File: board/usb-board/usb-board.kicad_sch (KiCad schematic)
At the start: 16 parts, among them J2 Conn_01x04_Pin, J3 USB_B_Micro, J4 Conn_01x04_Pin, SW1 SW_SPDT, U1 AMS1117-3.3, U2 STM32F103C8T6, Y1 8Mhz

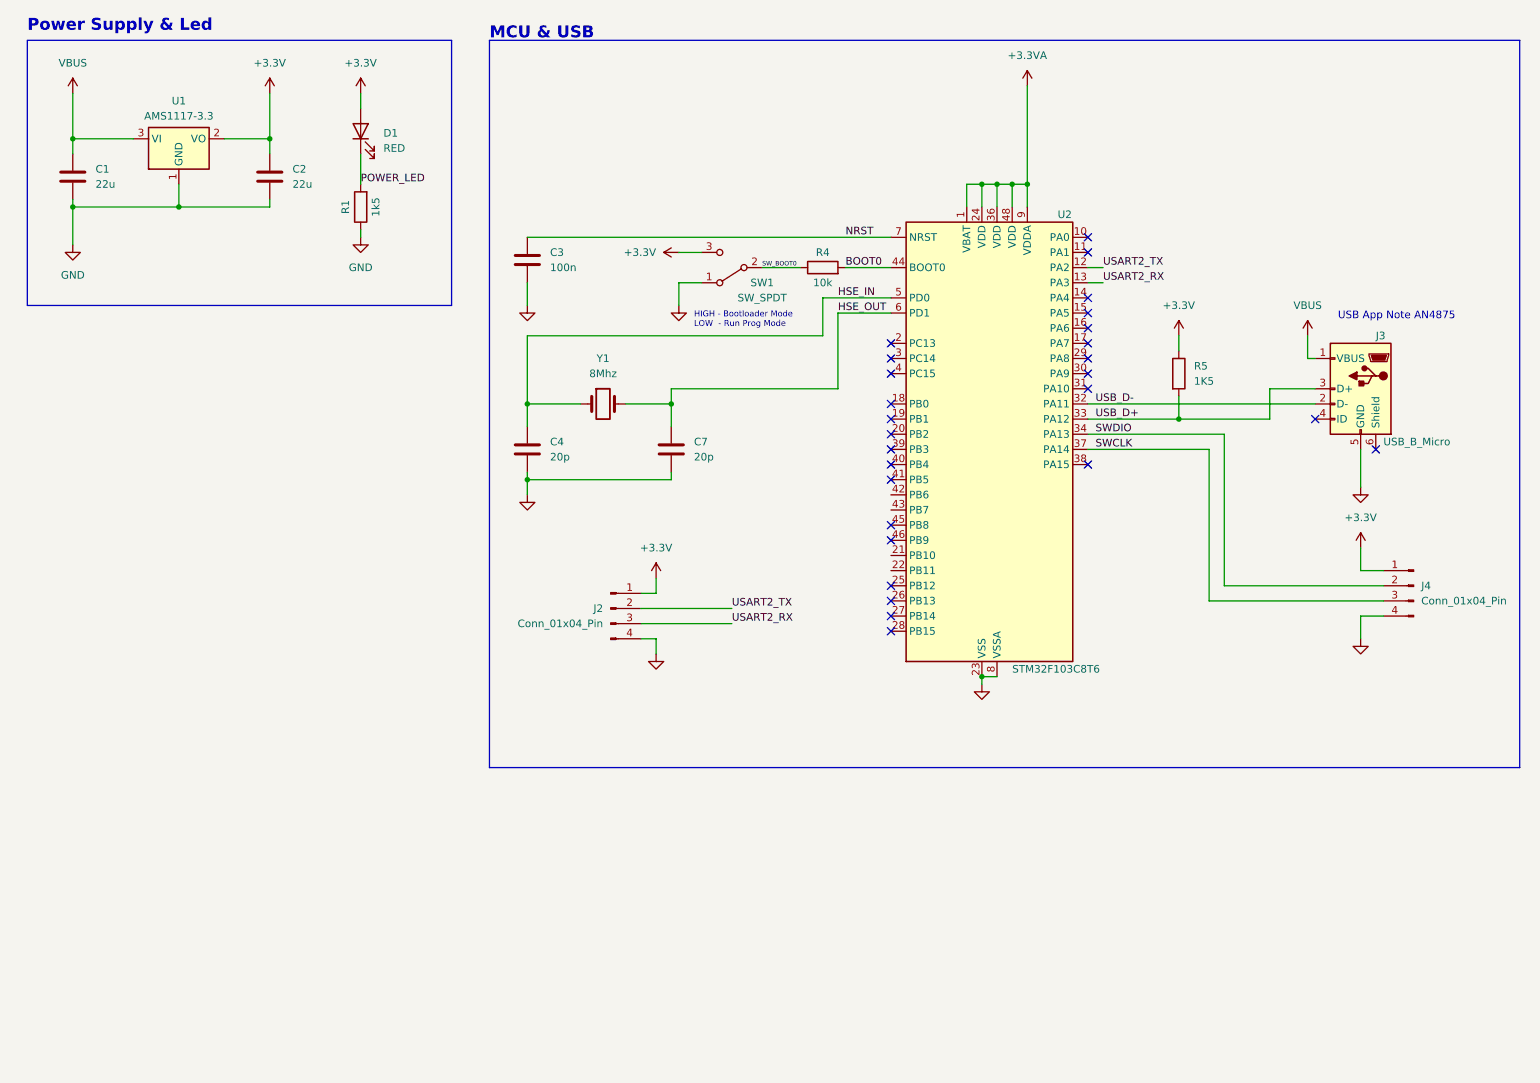
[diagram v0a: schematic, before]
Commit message: [ADD] Add transceiver on scheme for RS-485
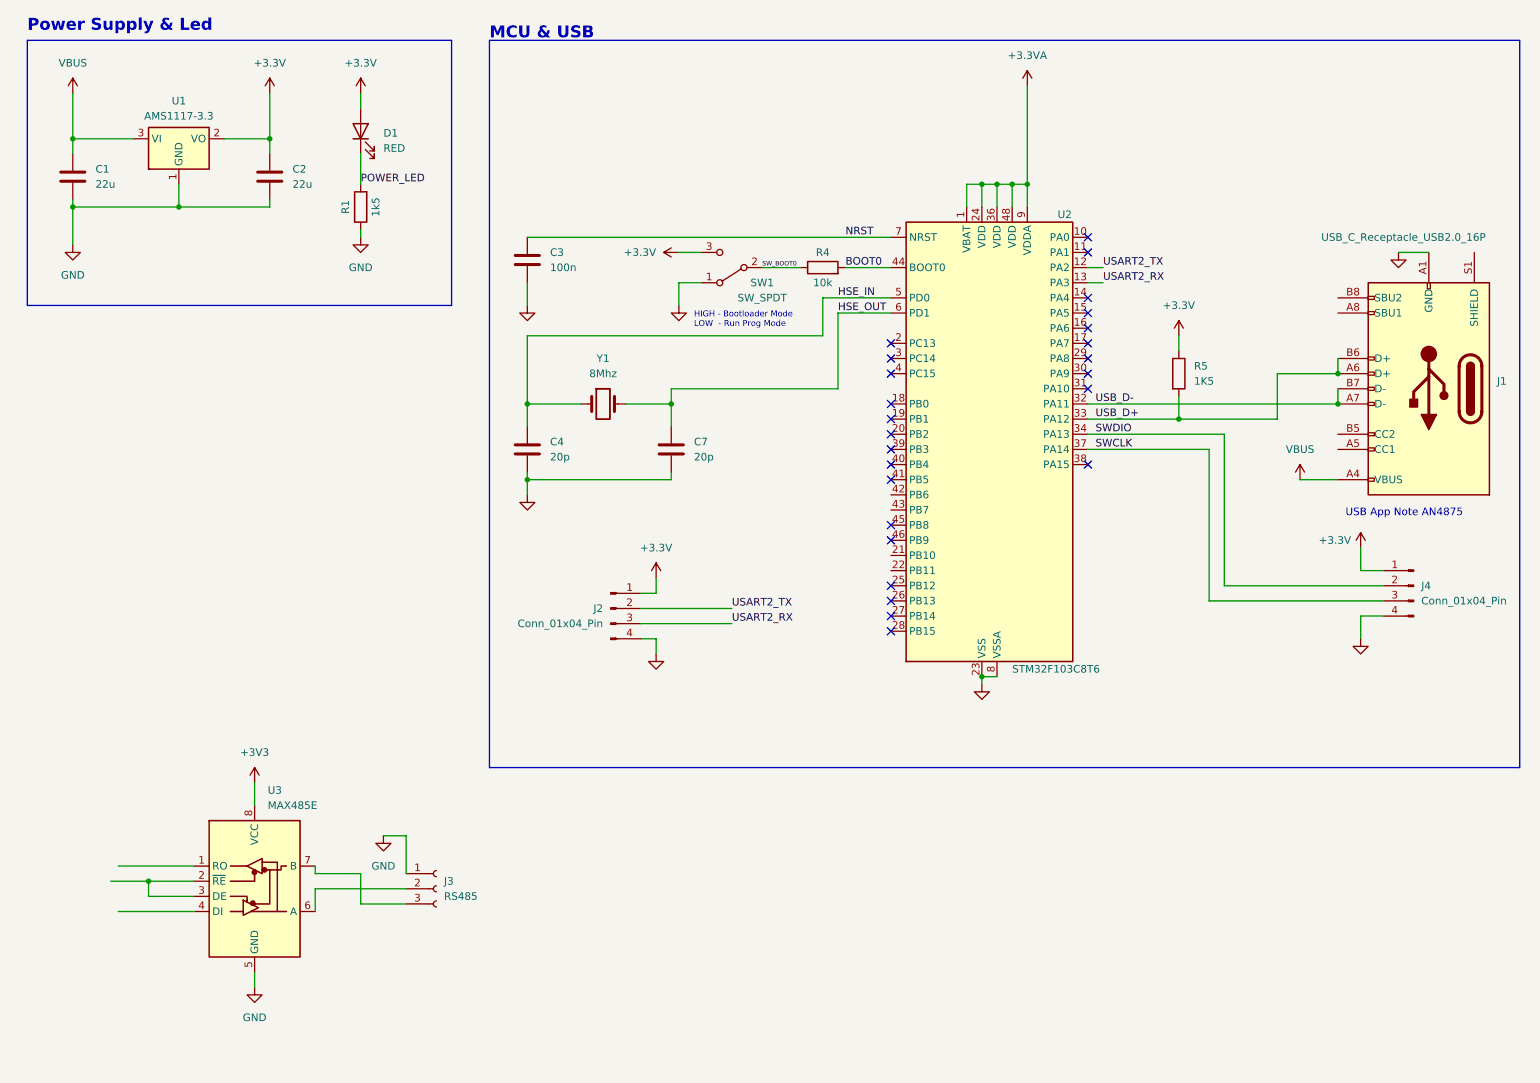
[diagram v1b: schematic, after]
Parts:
- removed J3: USB_B_Micro, Connector_USB:USB_Micro-B_Wuerth_629105150521, symbol Connector:USB_B_Micro
- added J1: USB_C_Receptacle_USB2.0_16P, Connector_USB:USB_C_Receptacle_GCT_USB4105-xx-A_16P_TopMnt_Horizontal, symbol Connector:USB_C_Receptacle_USB2.0_16P
- added J3: RS485, Connector_Phoenix_MSTB:PhoenixContact_MSTBA_2,5_3-G_1x03_P5.00mm_Horizontal, symbol Connector:Conn_01x03_Socket
- added U3: MAX485E, Package_SO:SO-8_3.9x4.9mm_P1.27mm, symbol Interface_UART:MAX485E
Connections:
- net GND: now also J1.A1 (GND), J1.A12 (GND), J1.B1 (GND), J1.B12 (GND), J3.1 (Pin_1), U3.5 (GND)
- net USB_D+: now also J1.A6 (D+), J1.B6 (D+)
- net USB_D-: now also J1.A7 (D-), J1.B7 (D-)
- net VBUS: now also J1.A4 (VBUS), J1.A9 (VBUS), J1.B4 (VBUS), J1.B9 (VBUS)
- new net: U3.2 (~{RE}), U3.3 (DE)
- new net: J3.2 (Pin_2), U3.6 (A)
- new net: J3.3 (Pin_3), U3.7 (B)
- new net +3V3: U3.8 (VCC)
- no-connect marks 27 -> 25

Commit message: [ENH] Enahnce board components
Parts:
- removed J2: Conn_01x04_Pin, Connector_PinHeader_2.54mm:PinHeader_1x04_P2.54mm_Vertical, symbol Connector:Conn_01x04_Pin
- removed SW1: SW_SPDT, Button_Switch_SMD:SW_SPDT_PCM12, symbol Switch:SW_SPDT
- added SW1: SW_DIP_x03, Button_Switch_SMD:SW_DIP_SPSTx03_Slide_6.7x9.18mm_W8.61mm_P2.54mm_LowProfile, symbol Switch:SW_DIP_x03
- J3: footprint Connector_Phoenix_MSTB:PhoenixContact_MSTBA_2,5_3-G_1x03_P5.00mm_Horizontal -> Connector_JST:JST_GH_SM03B-GHS-TB_1x03-1MP_P1.25mm_Horizontal
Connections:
- net SW_BOOT0 is gone; now on net GND: R4.1

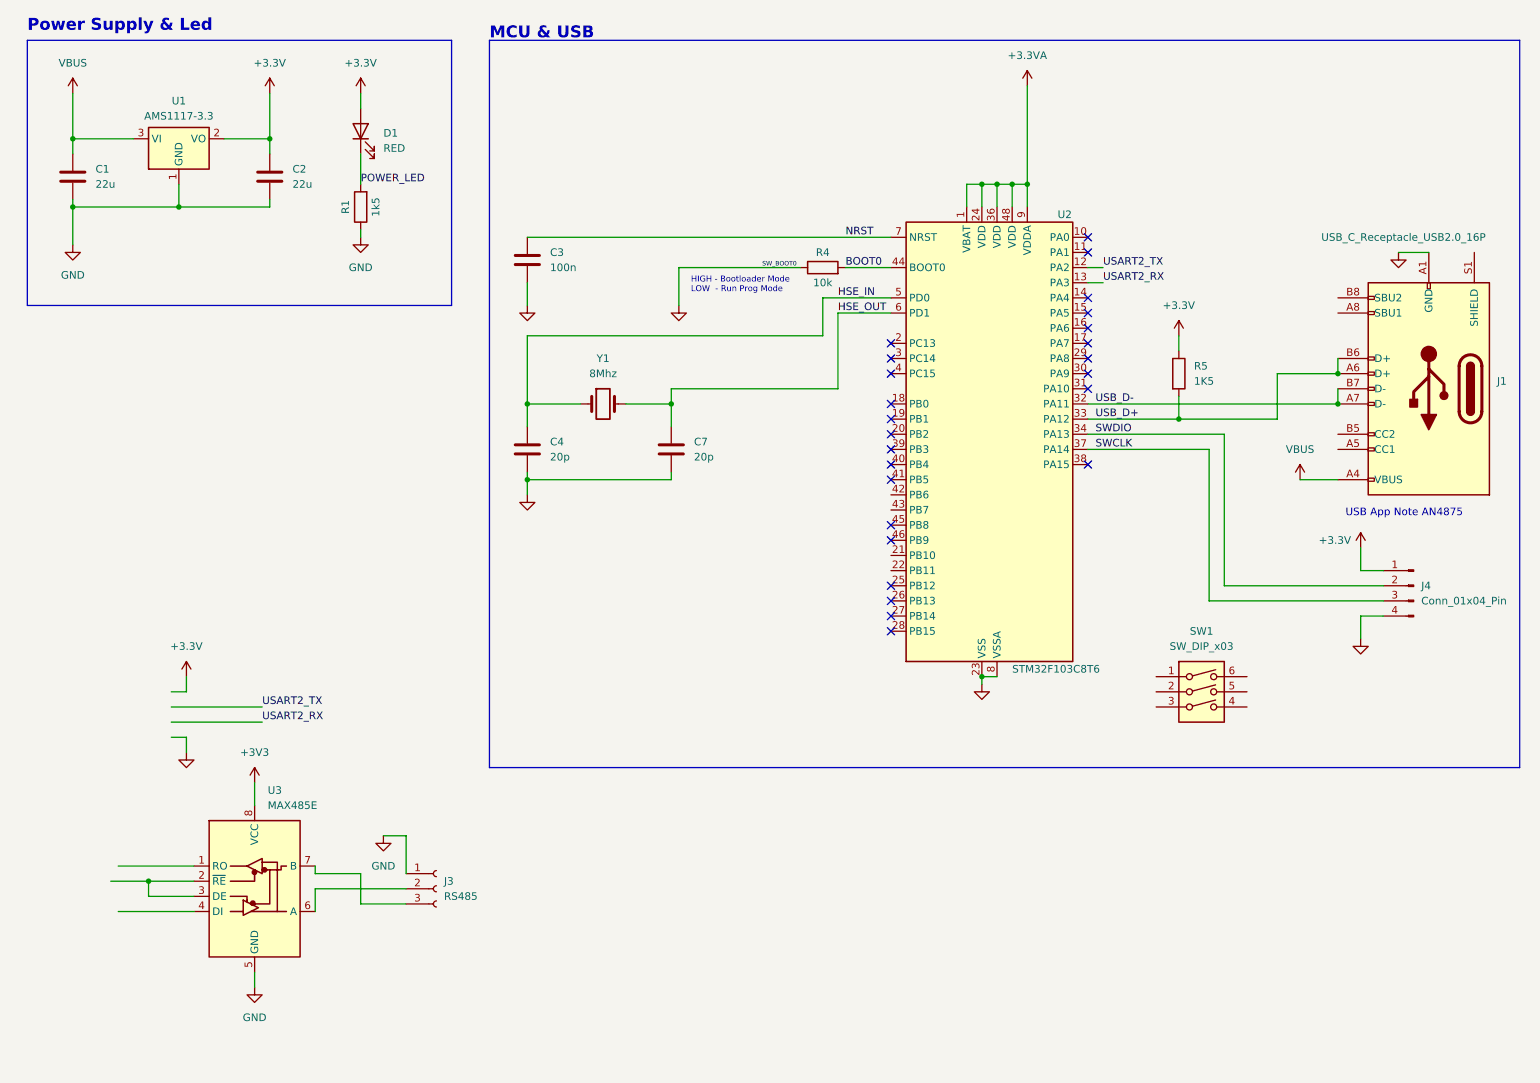
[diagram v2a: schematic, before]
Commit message: [UPD] Update board with 8 leds and enhance position of components on the board
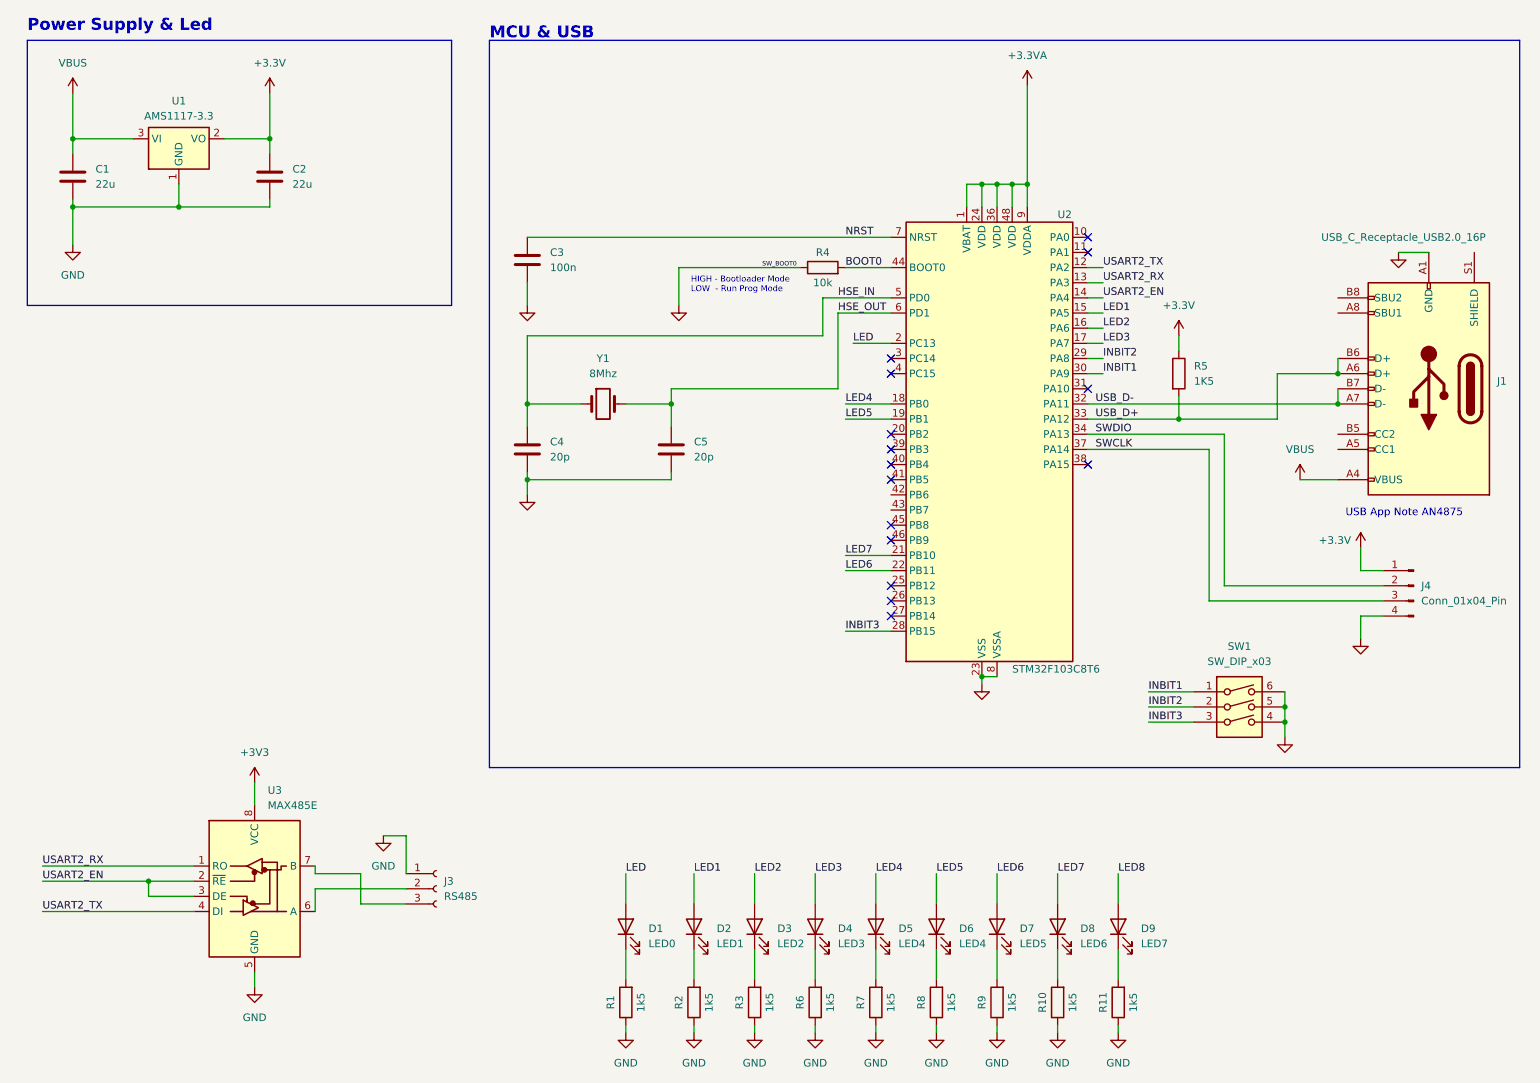
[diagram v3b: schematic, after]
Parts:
- added D2: LED1, LED_SMD:LED_1206_3216Metric_Pad1.42x1.75mm_HandSolder, symbol Device:LED
- added D3: LED2, LED_SMD:LED_1206_3216Metric_Pad1.42x1.75mm_HandSolder, symbol Device:LED
- added D4: LED3, LED_SMD:LED_1206_3216Metric_Pad1.42x1.75mm_HandSolder, symbol Device:LED
- added D5, D6: LED4, LED_SMD:LED_1206_3216Metric_Pad1.42x1.75mm_HandSolder, symbol Device:LED
- added D7: LED5, LED_SMD:LED_1206_3216Metric_Pad1.42x1.75mm_HandSolder, symbol Device:LED
- added D8: LED6, LED_SMD:LED_1206_3216Metric_Pad1.42x1.75mm_HandSolder, symbol Device:LED
- added D9: LED7, LED_SMD:LED_1206_3216Metric_Pad1.42x1.75mm_HandSolder, symbol Device:LED
- added R10, R11, R2, R3, R6, R7, R8, R9: 1k5, Resistor_SMD:R_1206_3216Metric_Pad1.30x1.75mm_HandSolder, symbol Device:R
- D1: value RED -> LED0; footprint LED_SMD:LED_0603_1608Metric -> LED_SMD:LED_1206_3216Metric_Pad1.42x1.75mm_HandSolder
- renumbered C7 to C5
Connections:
- net +3.3V: no longer D1.2 (A)
- net GND: now also SW1.4, SW1.5, SW1.6, R10.1, R11.1, R2.1, R3.1, R6.1, R7.1, R8.1, R9.1
- net USART2_RX: now also U3.1 (RO)
- net USART2_TX: now also U3.4 (DI)
- net INBIT1: now reaches SW1.1
- net INBIT1: now also U2.30 (PA9)
- net INBIT2: now reaches SW1.2
- net INBIT2: now also U2.29 (PA8)
- net INBIT3: now reaches SW1.3
- net INBIT3: now also U2.28 (PB15)
- net USART2_EN: now reaches U3.2 (~{RE}), U3.3 (DE)
- net USART2_EN: now also U2.14 (PA4)
- net LED1: now reaches U2.15 (PA5)
- net LED1: now also D2.2 (A)
- net LED2: now reaches U2.16 (PA6)
- net LED2: now also D3.2 (A)
- net LED3: now reaches U2.17 (PA7)
- net LED3: now also D4.2 (A)
- net LED4: now reaches U2.18 (PB0)
- net LED4: now also D5.2 (A)
- net LED5: now reaches U2.19 (PB1)
- net LED5: now also D6.2 (A)
- net LED: now reaches U2.2 (PC13)
- net LED: now also D1.2 (A)
- net LED7: now reaches U2.21 (PB10)
- net LED7: now also D8.2 (A)
- net LED6: now reaches U2.22 (PB11)
- net LED6: now also D7.2 (A)
- net POWER_LED: no longer names the net of D1.1 (K), R1.2
- new net: D3.1 (K), R3.2
- new net: D7.1 (K), R9.2
- new net: D5.1 (K), R7.2
- new net: D4.1 (K), R6.2
- new net: D9.1 (K), R11.2
- new net: D6.1 (K), R8.2
- new net: D2.1 (K), R2.2
- new net: D8.1 (K), R10.2
- new net LED8: D9.2 (A)
- no-connect marks 25 -> 15
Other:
- moved on the sheet: D1, R1, SW1

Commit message: [UPD] Update board with correct value for RESET pin
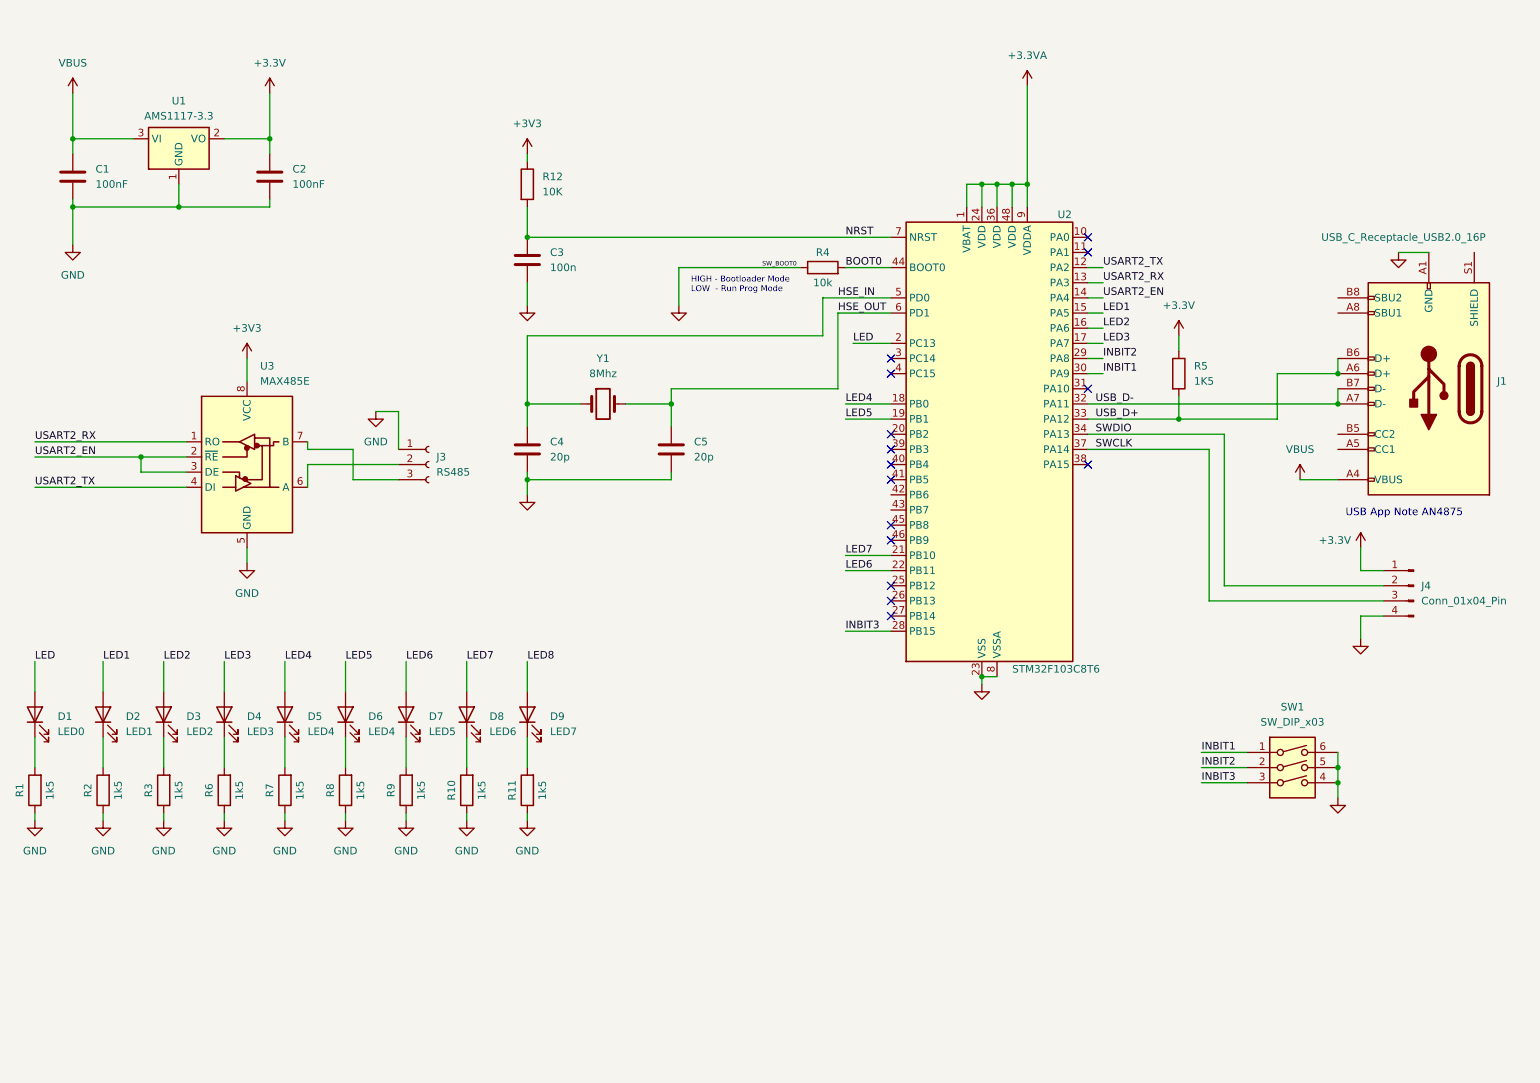
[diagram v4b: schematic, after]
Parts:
- added R12: 10K, Resistor_SMD:R_1206_3216Metric_Pad1.30x1.75mm_HandSolder, symbol Device:R
- C1, C2: value 22u -> 100nF
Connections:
- net +3V3: now also R12.1
- net NRST: now also R12.2
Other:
- note removed: "MCU & USB"
- note removed: "Power Supply & Led"
- moved on the sheet: D1, D2, D3, D4, D5, D6, D7, D8, D9, J3, R1, R10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
